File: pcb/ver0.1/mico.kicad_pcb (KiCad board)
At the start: 2 copper layers, 26.8 x 16 mm, 41 parts, among them J1 USB_A, J2 SWD Prog, U1 MCP1702, U2 MP23DB01HPTR, U3 W25Q128JV, U4 RP2040, U5 logo, Y1 H130B-12.000-20-3050-EXT-TR

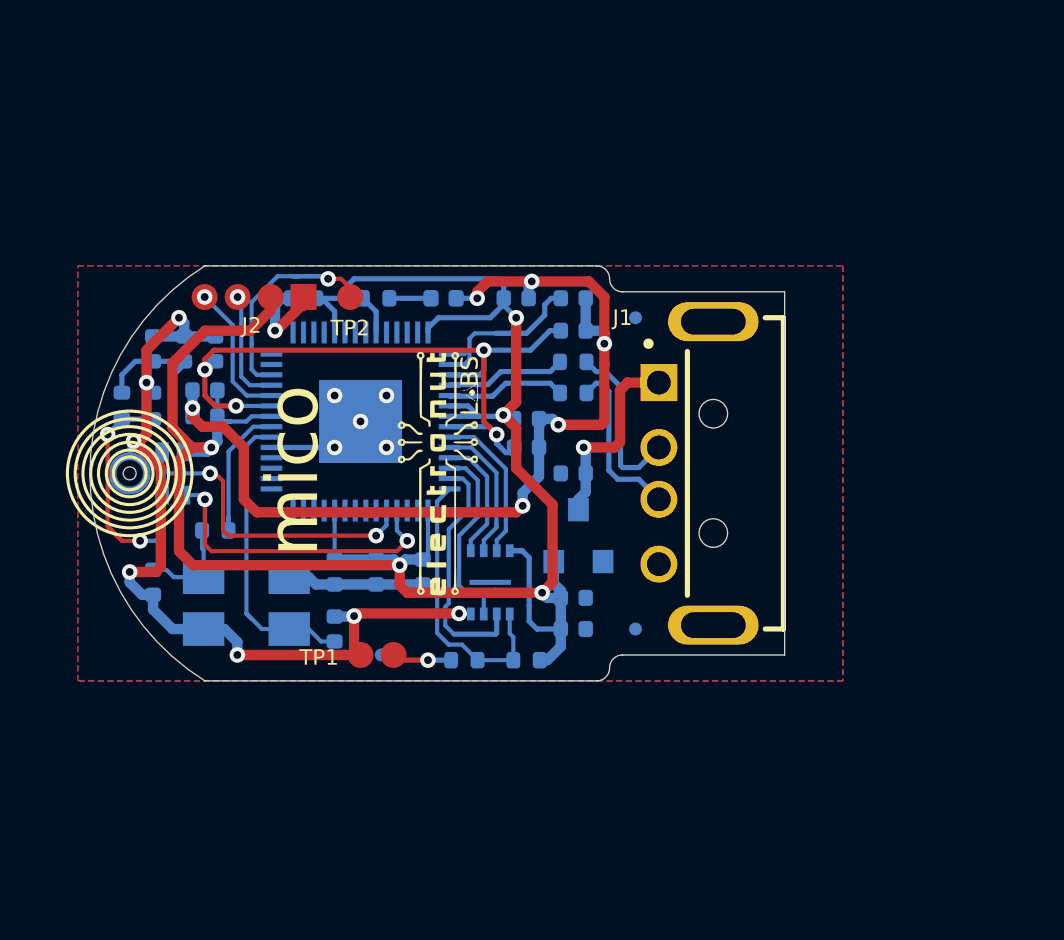
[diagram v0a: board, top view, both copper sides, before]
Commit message: hw revision with USB-C
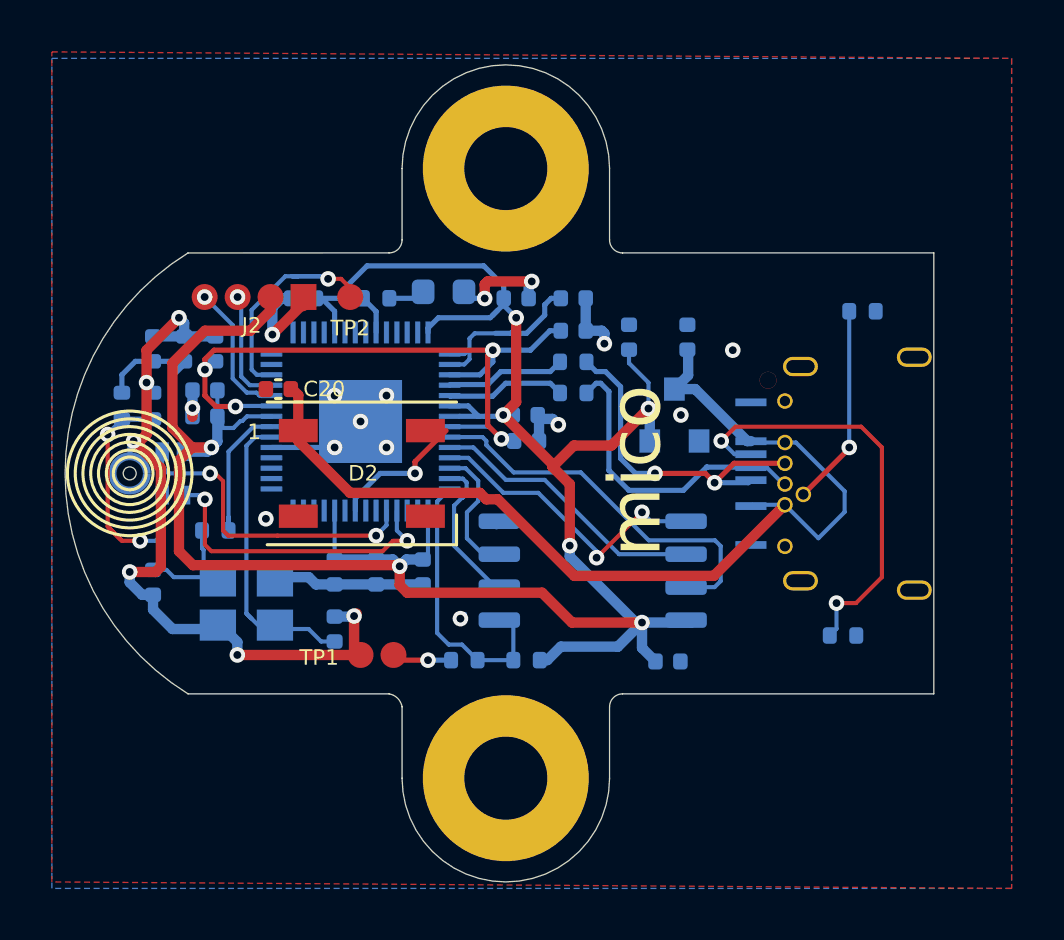
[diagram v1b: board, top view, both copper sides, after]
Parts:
- removed FID1, FID2, FID3: Fiducial, Fiducial:Fiducial_0.5mm_Mask1mm
- removed J1: USB_A, mico:USB-A
- removed U5: logo, mico:el_logo-9P4_3P1
- added C20: 0.1uF, Capacitor_SMD:C_0402_1005Metric, F.Cu at (127.2, 108.8)
- added D2: WS2812B, LED_SMD:LED_WS2812B_PLCC4_5.0x5.0mm_P3.2mm, F.Cu at (130.4, 112.0)
- added H1: MountingHole_Pad, MountingHole:MountingHole_3.2mm_M3_Pad, F.Cu at (136.0, 100.2)
- added H2: MountingHole_Pad, MountingHole:MountingHole_3.2mm_M3_Pad, F.Cu at (136.0, 123.8)
- added R10: 5.1k, Resistor_SMD:R_0402_1005Metric, B.Cu at (149.0, 118.2)
- added R9: 5.1k, Resistor_SMD:R_0402_1005Metric, B.Cu at (149.8, 105.8)
- added USB1: USB-306B, usbc:USB-TYPE-C-TH_USB-306B, B.Cu at (148.6, 112.0)
- D1: value APA3010SECK -> ~; footprint LED_SMD:LED_0402_1005Metric -> LED_SMD:LED_0603_1608Metric
- U3: footprint mico:PSON50P300X200X60-9N -> Package_SO:SOIC-8_5.275x5.275mm_P1.27mm
- Y1: footprint Crystal:Crystal_SMD_5032-4Pin_5.0x3.2mm -> Crystal:Crystal_SMD_3225-4Pin_3.2x2.5mm
- moved C5 10.3 mm to (140.8, 106.8), turned to 90 degrees
- moved C1 6.85 mm to (143.0, 106.8), turned to 90 degrees
- moved U1 5.94 mm to (142.5, 109.8)
- moved U3 3.98 mm to (139.3, 115.8), turned to 0 degrees
- moved C4 3.86 mm to (142.2, 119.2)
- moved C7 0.25 mm to (136.8, 110.8)
- moved D1 0.25 mm to (133.6, 105.0)
- moved C14 0.16 mm to (136.8, 109.8)
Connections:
- U4 pad 11: (no net) -> unconnected-(U4-GPIO8-Pad11)
- U4 pad 12: (no net) -> unconnected-(U4-GPIO9-Pad12)
- U4 pad 13: (no net) -> unconnected-(U4-GPIO10-Pad13)
- U4 pad 14: (no net) -> unconnected-(U4-GPIO11-Pad14)
- U4 pad 15: (no net) -> unconnected-(U4-GPIO12-Pad15)
- U4 pad 16: (no net) -> unconnected-(U4-GPIO13-Pad16)
- U4 pad 17: (no net) -> unconnected-(U4-GPIO14-Pad17)
- U4 pad 18: (no net) -> unconnected-(U4-GPIO15-Pad18)
- U4 pad 2: (no net) -> unconnected-(U4-GPIO0-Pad2)
- U4 pad 27: (no net) -> unconnected-(U4-GPIO16-Pad27)
- U4 pad 28: (no net) -> unconnected-(U4-GPIO17-Pad28)
- U4 pad 29: (no net) -> unconnected-(U4-GPIO18-Pad29)
- U4 pad 3: (no net) -> unconnected-(U4-GPIO1-Pad3)
- U4 pad 30: (no net) -> unconnected-(U4-GPIO19-Pad30)
- U4 pad 31: (no net) -> unconnected-(U4-GPIO20-Pad31)
- U4 pad 32: (no net) -> unconnected-(U4-GPIO21-Pad32)
- U4 pad 34: (no net) -> unconnected-(U4-GPIO22-Pad34)
- U4 pad 35: (no net) -> unconnected-(U4-GPIO23-Pad35)
- U4 pad 36: (no net) -> unconnected-(U4-GPIO24-Pad36)
- U4 pad 38: (no net) -> unconnected-(U4-GPIO26/ADC0-Pad38)
- U4 pad 39: (no net) -> unconnected-(U4-GPIO27/ADC1-Pad39)
- U4 pad 40: (no net) -> unconnected-(U4-GPIO28/ADC2-Pad40)
- U4 pad 41: (no net) -> unconnected-(U4-GPIO29/ADC3-Pad41)
- U4 pad 6: (no net) -> unconnected-(U4-GPIO4-Pad6)
- U4 pad 7: (no net) -> unconnected-(U4-GPIO5-Pad7)
- U4 pad 8: (no net) -> /NEOPIXEL_DIN
- U4 pad 9: (no net) -> unconnected-(U4-GPIO7-Pad9)
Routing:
- net VBUS: track 7.66 -> 39.8 mm, vias 1 -> 0
- net GND: track 85.2 -> 53.9 mm, vias 19 -> 21
- net Net-(USB1-CC1): track 0.00 -> 16.6 mm, vias 0 -> 2
- net +3V3: track 97.6 -> 111.5 mm, vias 5 -> 7
- net /QSPI_SD3: track 5.97 -> 14.8 mm
- net Net-(USB1-CC2): track 0.00 -> 7.83 mm, vias 0 -> 1
- net /QSPI_SD0: track 4.86 -> 12.4 mm, vias 0 -> 2
- net /USB0-D_N: track 6.58 -> 13.0 mm, vias 0 -> 2
- net /QSPI_SCLK: track 5.42 -> 11.5 mm
- net /USB0-D_P: track 6.58 -> 11.9 mm
- net /NEOPIXEL_DIN: track 0.00 -> 5.32 mm, vias 0 -> 1
- net /QSPI_SD1: track 9.52 -> 6.43 mm
- net /QSPI_SD2: track 7.43 -> 5.20 mm
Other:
- board size 26.8 x 16 mm -> 33.5 x 31.5 mm
- net class Default removed
- net class Diff_pair removed
- board text added: "JLCJLCJLCJLC"
- board text removed: "ver 0.1"
